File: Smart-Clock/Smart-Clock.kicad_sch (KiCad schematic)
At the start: 14 parts, among them SW2 SW_SPDT, SW3 RotaryEncoder, U1 ESP32-WROOM-32D

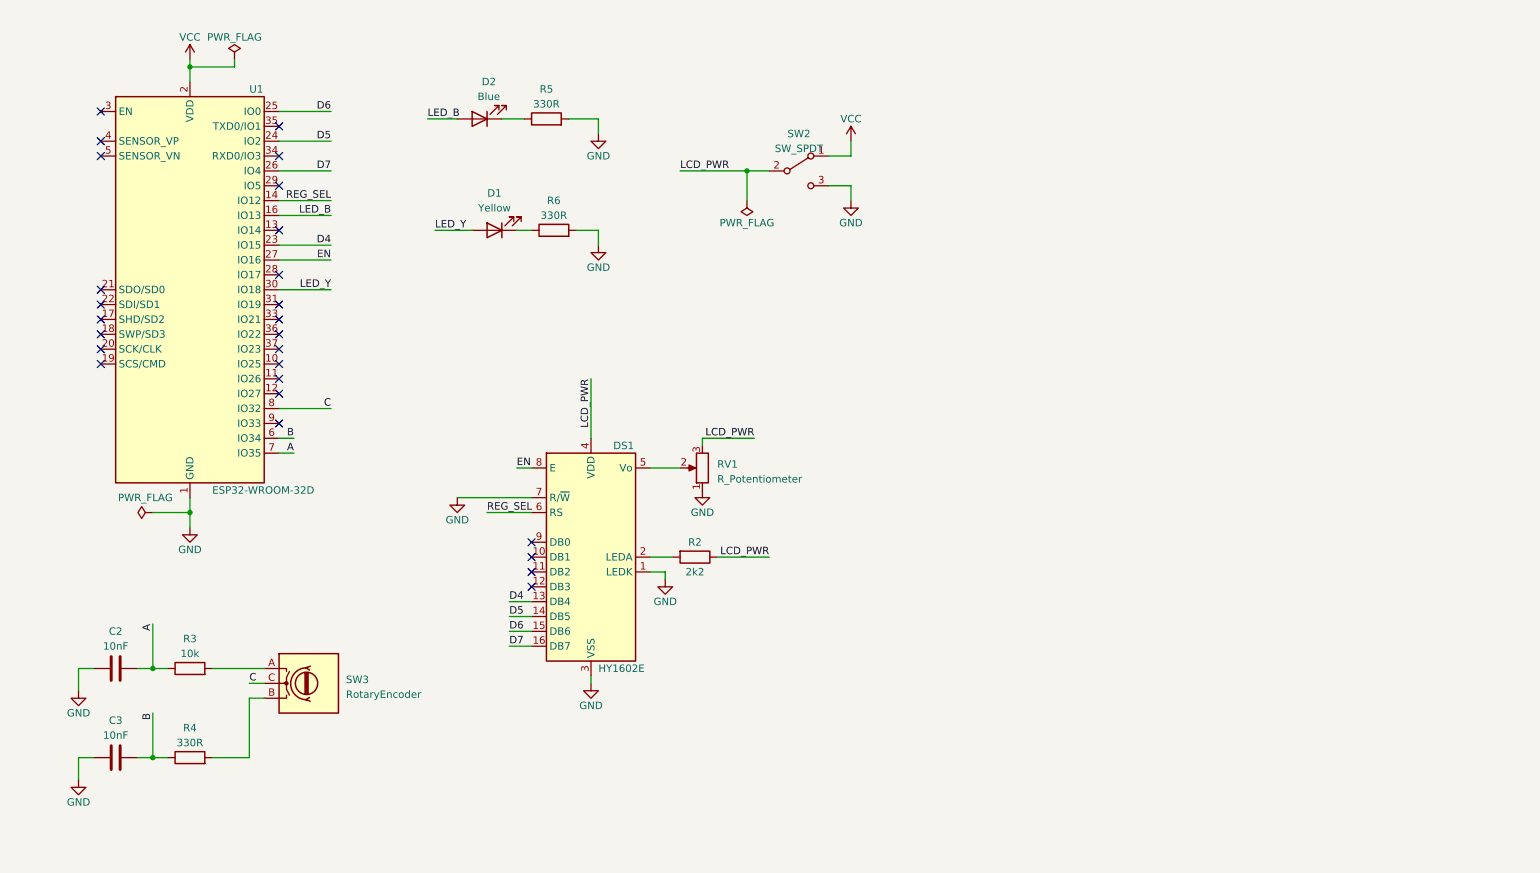
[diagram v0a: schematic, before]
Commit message: Fixed rotary encoder circuit.
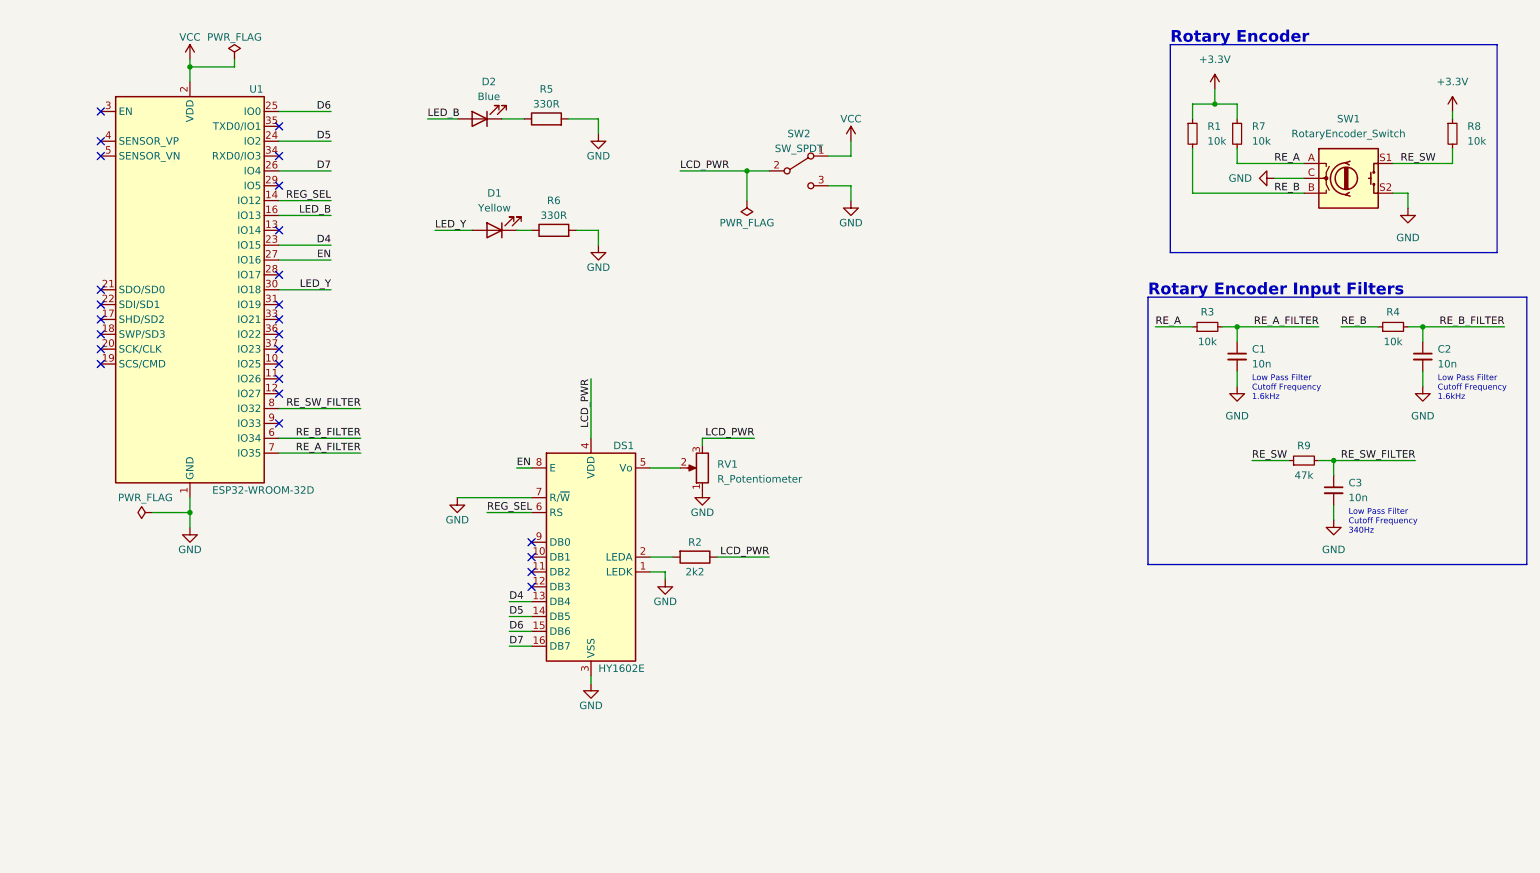
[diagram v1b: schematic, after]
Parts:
- removed C2, C3: 10nF, Capacitor_SMD:C_1206_3216Metric_Pad1.33x1.80mm_HandSolder, symbol Device:C
- removed R3: 10k, Resistor_THT:R_Axial_Power_L25.0mm_W9.0mm_P30.48mm, symbol Device:R
- removed R4: 330R, Resistor_THT:R_Axial_Power_L25.0mm_W9.0mm_P30.48mm, symbol Device:R
- removed SW3: RotaryEncoder, Rotary_Encoder:RotaryEncoder_Bourns_Horizontal_PEC09-2xxxF-Nxxxx, symbol Device:RotaryEncoder
- added C1, C2, C3: 10n, symbol Device:C_Small
- added R1, R3, R4, R7, R8: 10k, symbol Device:R_Small
- added R9: 47k, symbol Device:R_Small
- added SW1: RotaryEncoder_Switch, symbol Device:RotaryEncoder_Switch
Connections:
- net GND: now also C1.2, C2.2, C3.2, SW1.C, SW1.S2
- net A renamed RE_A_FILTER
- net RE_A_FILTER: now also C1.1, R3.2
- net B renamed RE_B_FILTER
- net RE_B_FILTER: now also C2.1, R4.2
- net C renamed RE_SW_FILTER
- net RE_SW_FILTER: now also C3.1, R9.2
- new net +3.3V: R1.1, R7.1, R8.1
- new net RE_A: R3.1, R7.2, SW1.A
- new net RE_B: R1.2, R4.1, SW1.B
- new net RE_SW: R8.2, R9.1, SW1.S1
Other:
- note added: "Low Pass Filter Cutoff Frequency 1.6kHz"
- note added: "Low Pass Filter Cutoff Frequency 340Hz"
- note added: "Rotary Encoder"
- note added: "Rotary Encoder Input Filters"

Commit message: Updated drawing sheets and title blocks.
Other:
- company: (none) -> Trion Embedded
- title: (none) -> Smart Clock Hardware
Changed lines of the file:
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@@
 (kicad_sch (version 20230121) (generator eeschema)
   (paper "A4")
+  (title_block
+    (title "Smart Clock Hardware")
+    (date "2023-07-11")
+    (rev "v0.1")
+    (company "Trion Embedded")
+    (comment 1 "Design by: Emirhan Yuksel ")
+    (comment 2 "Revised by: Bahtiyar Bayram")
+  )
   (junction (at 259.08 69.85) (diameter 0) (color 0 0 0 0)
   )

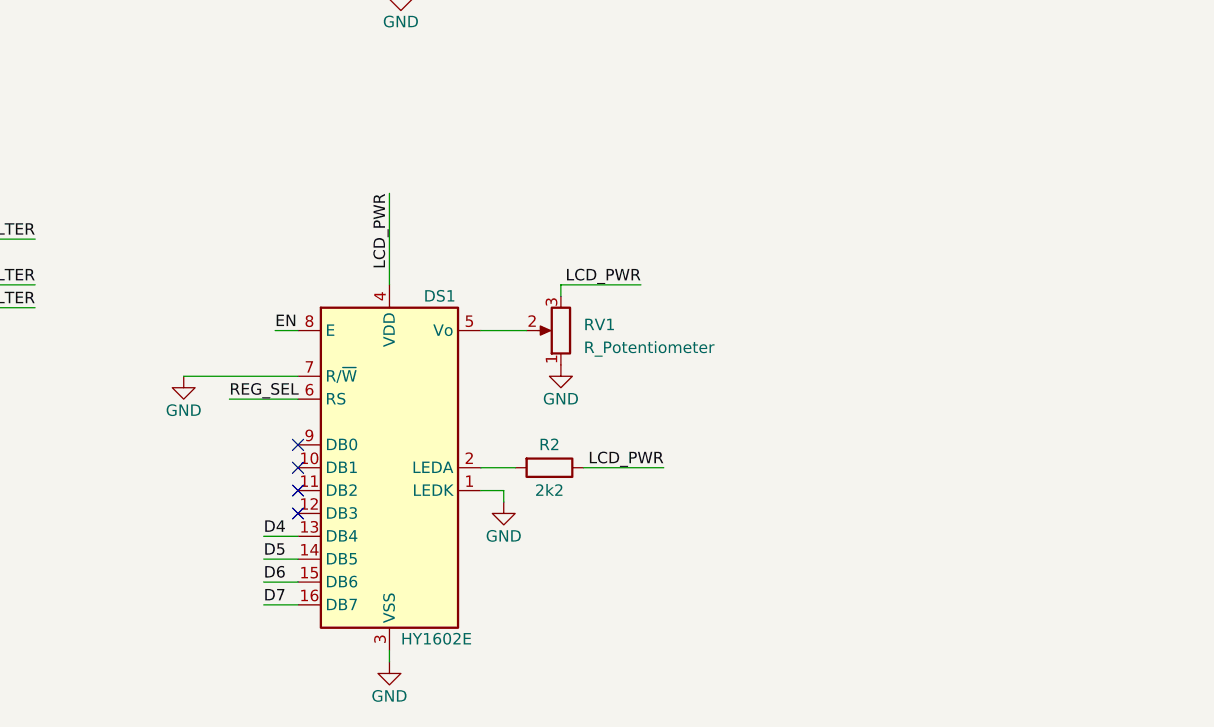
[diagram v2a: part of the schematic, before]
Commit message: Updated LCD Display.
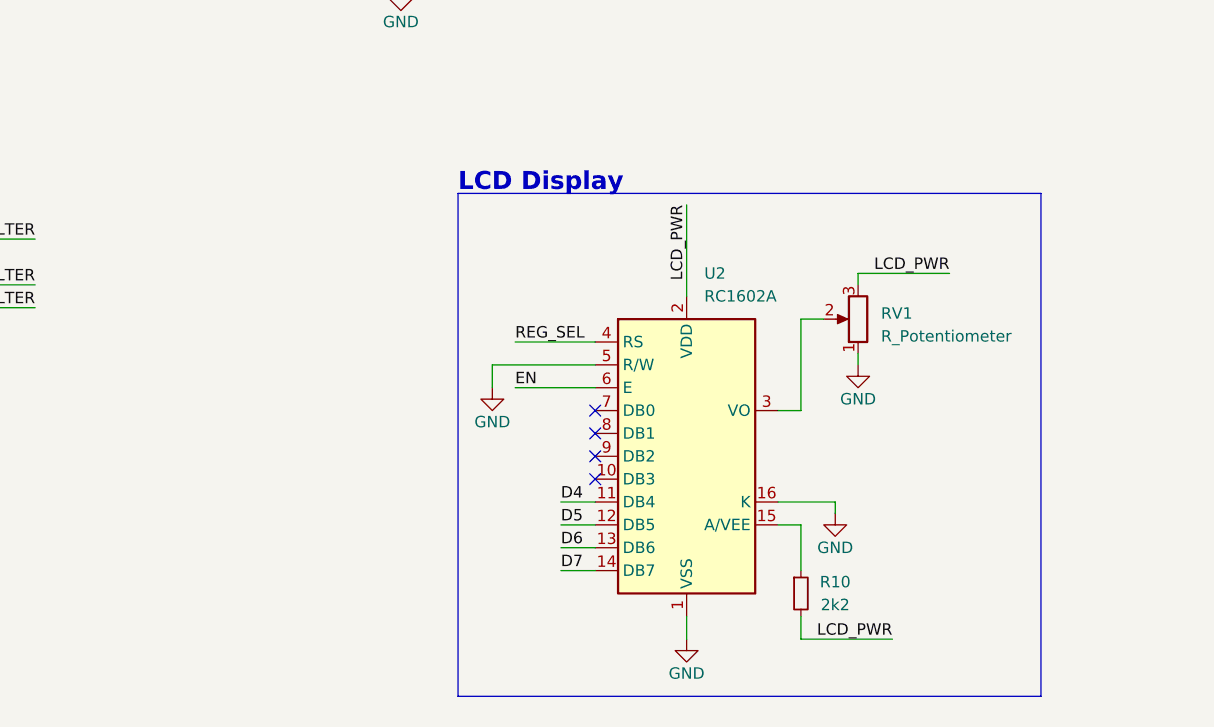
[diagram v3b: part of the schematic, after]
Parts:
- removed DS1: HY1602E, Display:HY1602E, symbol Display_Character:HY1602E
- removed R2: 2k2, Resistor_THT:R_Axial_Power_L25.0mm_W9.0mm_P30.48mm, symbol Device:R
- added R10: 2k2, symbol Device:R_Small
- added U2: RC1602A, Display:RC1602A, symbol Display_Character:RC1602A
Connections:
- net D4: now also U2.11 (DB4)
- net D5: now also U2.12 (DB5)
- net D6: now also U2.13 (DB6)
- net D7: now also U2.14 (DB7)
- net EN: now also U2.6 (E)
- net GND: now also U2.1 (VSS), U2.16 (K), U2.5 (R/W)
- net LCD_PWR: now also R10.2, U2.2 (VDD)
- net REG_SEL: now also U2.4 (RS)
- net at RV1.2: now also U2.3 (VO)
- new net: R10.1, U2.15 (A/VEE)
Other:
- note added: "LCD Display"
- moved on the sheet: RV1

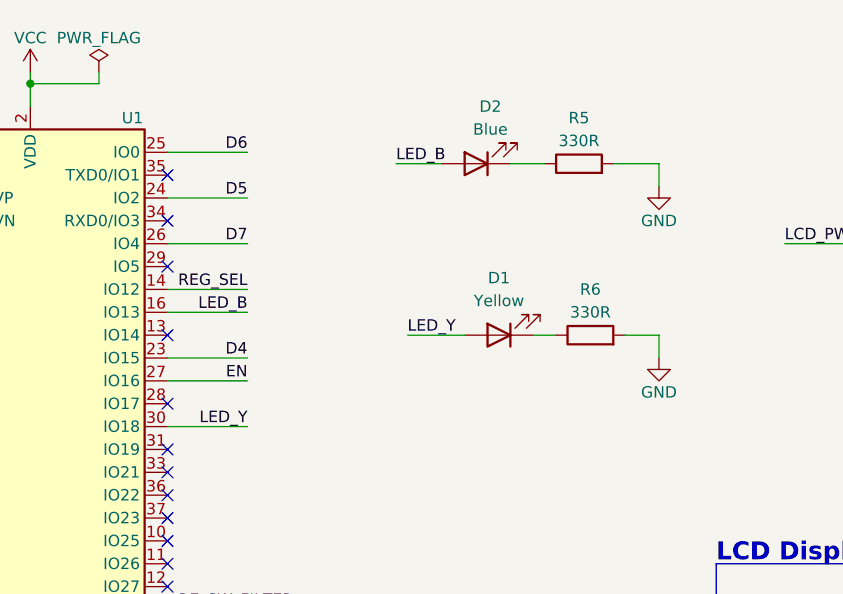
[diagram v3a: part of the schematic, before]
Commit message: Deleted unused leds.
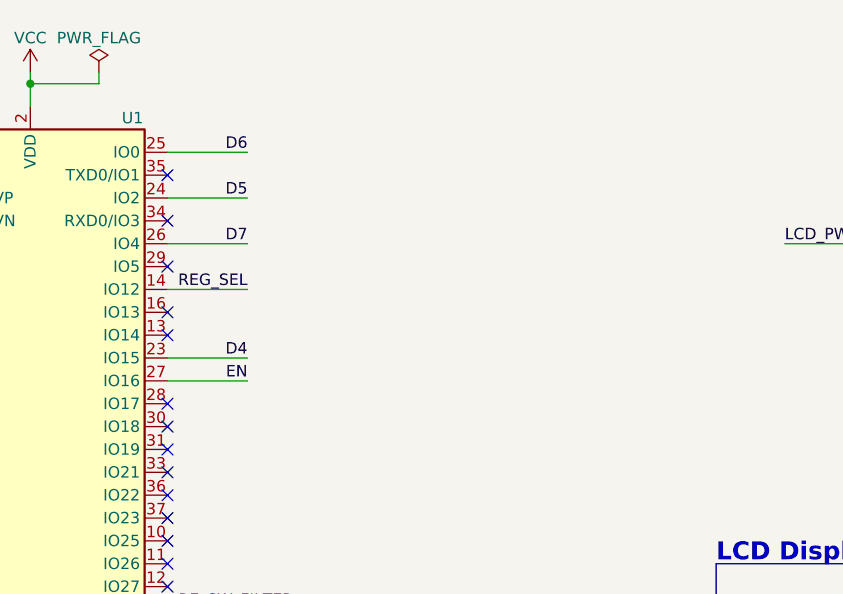
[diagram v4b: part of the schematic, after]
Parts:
- removed D1: Yellow, LED_THT:LED_D5.0mm_Horizontal_O3.81mm_Z15.0mm, symbol Device:LED
- removed D2: Blue, LED_THT:LED_D5.0mm_Horizontal_O3.81mm_Z15.0mm, symbol Device:LED
- removed R5, R6: 330R, Resistor_THT:R_Axial_Power_L25.0mm_W9.0mm_P30.48mm, symbol Device:R
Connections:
- net LED_B: no longer names the net of U1.16 (IO13)
- net LED_Y: no longer names the net of U1.30 (IO18)
- no-connect marks 26 -> 28
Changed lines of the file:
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@@
   (no_connect (at 63.5 45.72))
   (no_connect (at 139.7 102.87))
+  (no_connect (at 63.5 63.5))
   (no_connect (at 139.7 110.49))
   (no_connect (at 63.5 73.66))
   (no_connect (at 33.02 63.5))
   (no_connect (at 33.02 40.64))
+  (no_connect (at 63.5 50.8))
   (no_connect (at 33.02 73.66))
   (no_connect (at 63.5 68.58))
@@
     (stroke (width 0) (type default))
   )
-  (wire (pts (xy 113.03 34.29) (xy 118.11 34.29))
-    (stroke (width 0) (type default))
-  )
   (wire (pts (xy 135.89 118.11) (xy 139.7 118.11))
     (stroke (width 0) (type default))
@@
     (stroke (width 0) (type default))
   )
-  (wire (pts (xy 96.52 53.34) (xy 90.17 53.34))
-    (stroke (width 0) (type default))
-  )
   (wire (pts (xy 254 41.91) (xy 264.16 41.91))
     (stroke (width 0) (type default))
@@
     (stroke (width 0) (type default))
   )
-  (wire (pts (xy 93.98 34.29) (xy 88.9 34.29))
-    (stroke (width 0) (type default))
-  )
   (wire (pts (xy 243.84 95.25) (xy 243.84 92.71))
     (stroke (width 0) (type default))
@@
     (stroke (width 0) (type default))
   )
-  (wire (pts (xy 63.5 63.5) (xy 72.39 63.5))
-    (stroke (width 0) (type default))
-  )
   (wire (pts (xy 63.5 43.18) (xy 72.39 43.18))
     (stroke (width 0) (type default))
@@
     (stroke (width 0) (type default))
   )
-  (wire (pts (xy 114.3 53.34) (xy 118.11 53.34))
-    (stroke (width 0) (type default))
-  )
   (wire (pts (xy 135.89 120.65) (xy 139.7 120.65))
     (stroke (width 0) (type default))
@@
     (stroke (width 0) (type default))
   )
-  (wire (pts (xy 63.5 50.8) (xy 72.39 50.8))
-    (stroke (width 0) (type default))
-  )
   (wire (pts (xy 132.08 43.18) (xy 143.51 43.18))
     (stroke (width 0) (type default))
@@
     (stroke (width 0) (type default))
   )
-  (wire (pts (xy 118.11 34.29) (xy 118.11 36.83))
-    (stroke (width 0) (type default))
-  )
   (wire (pts (xy 227.33 77.47) (xy 227.33 80.01))
     (stroke (width 0) (type default))
@@
     (stroke (width 0) (type default))
   )
-  (wire (pts (xy 118.11 53.34) (xy 118.11 55.88))
-    (stroke (width 0) (type default))
-  )
   (wire (pts (xy 149.86 80.01) (xy 149.86 90.17))
     (stroke (width 0) (type default))
@@
   )
   (wire (pts (xy 179.07 87.63) (xy 168.91 87.63))
-    (stroke (width 0) (type default))
-  )
-  (wire (pts (xy 101.6 34.29) (xy 105.41 34.29))
-    (stroke (width 0) (type default))
-  )
-  (wire (pts (xy 104.14 53.34) (xy 106.68 53.34))
     (stroke (width 0) (type default))
   )
@@
     (effects (font (size 1.27 1.27)) (justify right bottom))
   )
-  (label "LED_Y" (at 72.39 63.5 180) (fields_autoplaced)
-    (effects (font (size 1.27 1.27)) (justify right bottom))
-  )
   (label "D4" (at 135.89 113.03 0) (fields_autoplaced)
     (effects (font (size 1.27 1.27)) (justify left bottom))
@@
     (effects (font (size 1.27 1.27)) (justify right bottom))
   )
-  (label "LED_B" (at 72.39 50.8 180) (fields_autoplaced)
-    (effects (font (size 1.27 1.27)) (justify right bottom))
-  )
   (label "LCD_PWR" (at 179.07 87.63 180) (fields_autoplaced)
     (effects (font (size 1.27 1.27)) (justify right bottom))
@@
     (effects (font (size 1.27 1.27)) (justify right bottom))
   )
-  (label "LED_B" (at 88.9 34.29 0) (fields_autoplaced)
-    (effects (font (size 1.27 1.27)) (justify left bottom))
-  )
   (label "D6" (at 72.39 33.02 180) (fields_autoplaced)
     (effects (font (size 1.27 1.27)) (justify right bottom))
@@
     (effects (font (size 1.27 1.27)) (justify right bottom))
   )
-  (label "LED_Y" (at 90.17 53.34 0) (fields_autoplaced)
-    (effects (font (size 1.27 1.27)) (justify left bottom))
-  )
   (label "RE_SW" (at 229.87 92.71 0) (fields_autoplaced)
     (effects (font (size 1.27 1.27)) (justify left bottom))
@@
   (label "RE_B_FILTER" (at 273.05 69.85 180) (fields_autoplaced)
     (effects (font (size 1.27 1.27)) (justify right bottom))
-  )
-  (symbol (lib_id "Device:LED") (at 97.79 34.29 180) (unit 1)
-    (in_bom yes) (on_board yes) (dnp no) (fields_autoplaced)
-    (property "Reference" "D2" (at 99.3775 27.94 0)
-      (effects (font (size 1.27 1.27)))
-    )
-    (property "Value" "Blue" (at 99.3775 30.48 0)
-      (effects (font (size 1.27 1.27)))
-    )
-    (property "Footprint" "LED_THT:LED_D5.0mm_Horizontal_O3.81mm_Z15.0mm" (at 97.79 34.29 0)
-      (effects (font (size 1.27 1.27)) hide)
-    )
-    (property "Datasheet" "~" (at 97.79 34.29 0)
-      (effects (font (size 1.27 1.27)) hide)
-    )
-    (pin "1")
-    (pin "2")
-    (instances
-      (project "Smart-Clock"
-        (path "/e34c15c6-e607-4cb4-85cc-7ea553cda6e2"
-          (reference "D2") (unit 1)
-        )
-      )
-    )
-  )
-  (symbol (lib_id "power:GND") (at 118.11 55.88 0) (unit 1)
-    (in_bom yes) (on_board yes) (dnp no)
-    (property "Reference" "#PWR04" (at 118.11 62.23 0)
-      (effects (font (size 1.27 1.27)) hide)
-    )
-    (property "Value" "GND" (at 118.11 59.69 0)
-      (effects (font (size 1.27 1.27)))
-    )
-    (property "Footprint" "" (at 118.11 55.88 0)
-      (effects (font (size 1.27 1.27)) hide)
-    )
-    (property "Datasheet" "" (at 118.11 55.88 0)
-      (effects (font (size 1.27 1.27)) hide)
-    )
-    (pin "1")
-    (instances
-      (project "Smart-Clock"
-        (path "/e34c15c6-e607-4cb4-85cc-7ea553cda6e2"
-          (reference "#PWR04") (unit 1)
-        )
-      )
-    )
   )
   (symbol (lib_id "power:GND") (at 256.54 49.53 0) (unit 1)
@@
     )
   )
-  (symbol (lib_id "Device:R") (at 109.22 34.29 90) (unit 1)
-    (in_bom yes) (on_board yes) (dnp no) (fields_autoplaced)
-    (property "Reference" "R5" (at 109.22 29.21 90)
-      (effects (font (size 1.27 1.27)))
-    )
-    (property "Value" "330R" (at 109.22 31.75 90)
-      (effects (font (size 1.27 1.27)))
-    )
-    (property "Footprint" "Resistor_THT:R_Axial_Power_L25.0mm_W9.0mm_P30.48mm" (at 109.22 36.068 90)
-      (effects (font (size 1.27 1.27)) hide)
-    )
-    (property "Datasheet" "~" (at 109.22 34.29 0)
-      (effects (font (size 1.27 1.27)) hide)
-    )
-    (pin "1")
-    (pin "2")
-    (instances
-      (project "Smart-Clock"
-        (path "/e34c15c6-e607-4cb4-85cc-7ea553cda6e2"
-          (reference "R5") (unit 1)
-        )
-      )
-    )
-  )
-  (symbol (lib_id "Device:R") (at 110.49 53.34 90) (unit 1)
-    (in_bom yes) (on_board yes) (dnp no) (fields_autoplaced)
-    (property "Reference" "R6" (at 110.49 48.26 90)
-      (effects (font (size 1.27 1.27)))
-    )
-    (property "Value" "330R" (at 110.49 50.8 90)
-      (effects (font (size 1.27 1.27)))
-    )
-    (property "Footprint" "Resistor_THT:R_Axial_Power_L25.0mm_W9.0mm_P30.48mm" (at 110.49 55.118 90)
-      (effects (font (size 1.27 1.27)) hide)
-    )
-    (property "Datasheet" "~" (at 110.49 53.34 0)
-      (effects (font (size 1.27 1.27)) hide)
-    )
-    (pin "1")
-    (pin "2")
-    (instances
-      (project "Smart-Clock"
-        (path "/e34c15c6-e607-4cb4-85cc-7ea553cda6e2"
-          (reference "R6") (unit 1)
-        )
-      )
-    )
-  )
   (symbol (lib_id "power:PWR_FLAG") (at 41.91 101.6 90) (unit 1)
     (in_bom yes) (on_board yes) (dnp no) (fields_autoplaced)
@@
         (path "/e34c15c6-e607-4cb4-85cc-7ea553cda6e2"
           (reference "#PWR010") (unit 1)
-        )
-      )
-    )
-  )
-  (symbol (lib_id "Device:LED") (at 100.33 53.34 180) (unit 1)
-    (in_bom yes) (on_board yes) (dnp no)
-    (property "Reference" "D1" (at 100.33 46.99 0)
-      (effects (font (size 1.27 1.27)))
-    )
-    (property "Value" "Yellow" (at 100.33 49.53 0)
-      (effects (font (size 1.27 1.27)))
-    )
-    (property "Footprint" "LED_THT:LED_D5.0mm_Horizontal_O3.81mm_Z15.0mm" (at 100.33 53.34 0)
-      (effects (font (size 1.27 1.27)) hide)
-    )
-    (property "Datasheet" "~" (at 100.33 53.34 0)
-      (effects (font (size 1.27 1.27)) hide)
-    )
-    (pin "1")
-    (pin "2")
-    (instances
-      (project "Smart-Clock"
-        (path "/e34c15c6-e607-4cb4-85cc-7ea553cda6e2"
-          (reference "D1") (unit 1)
         )
       )
@@
         )
       )
-    )
-  )
-  (symbol (lib_id "power:GND") (at 118.11 36.83 0) (unit 1)
-    (in_bom yes) (on_board yes) (dnp no)
-    (property "Reference" "#PWR012" (at 118.11 43.18 0)
-      (effects (font (size 1.27 1.27)) hide)
-    )
-    (property "Value" "GND" (at 118.11 40.64 0)
-      (effects (font (size 1.27 1.27)))
-    )
-    (property "Footprint" "" (at 118.11 36.83 0)
-      (effects (font (size 1.27 1.27)) hide)
-    )
-    (property "Datasheet" "" (at 118.11 36.83 0)
-      (effects (font (size 1.27 1.27)) hide)
-    )
-    (pin "1")
-    (instances
-      (project "Smart-Clock"
-        (path "/e34c15c6-e607-4cb4-85cc-7ea553cda6e2"
-          (reference "#PWR012") (unit 1)
-        )
-      )
